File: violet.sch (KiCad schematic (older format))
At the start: 47 parts, among them J1 NEIGHBOR1, J10 Conn_01x08, J2 NEIGHBOR2, J3 NEIGHBOR1, J4 BONUS_ROW, J5 NEIGHBOR2, J6 NEIGHBOR1, J7 BONUS_ROW, J8 BONUS_ROW, J9 NEIGHBOR2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

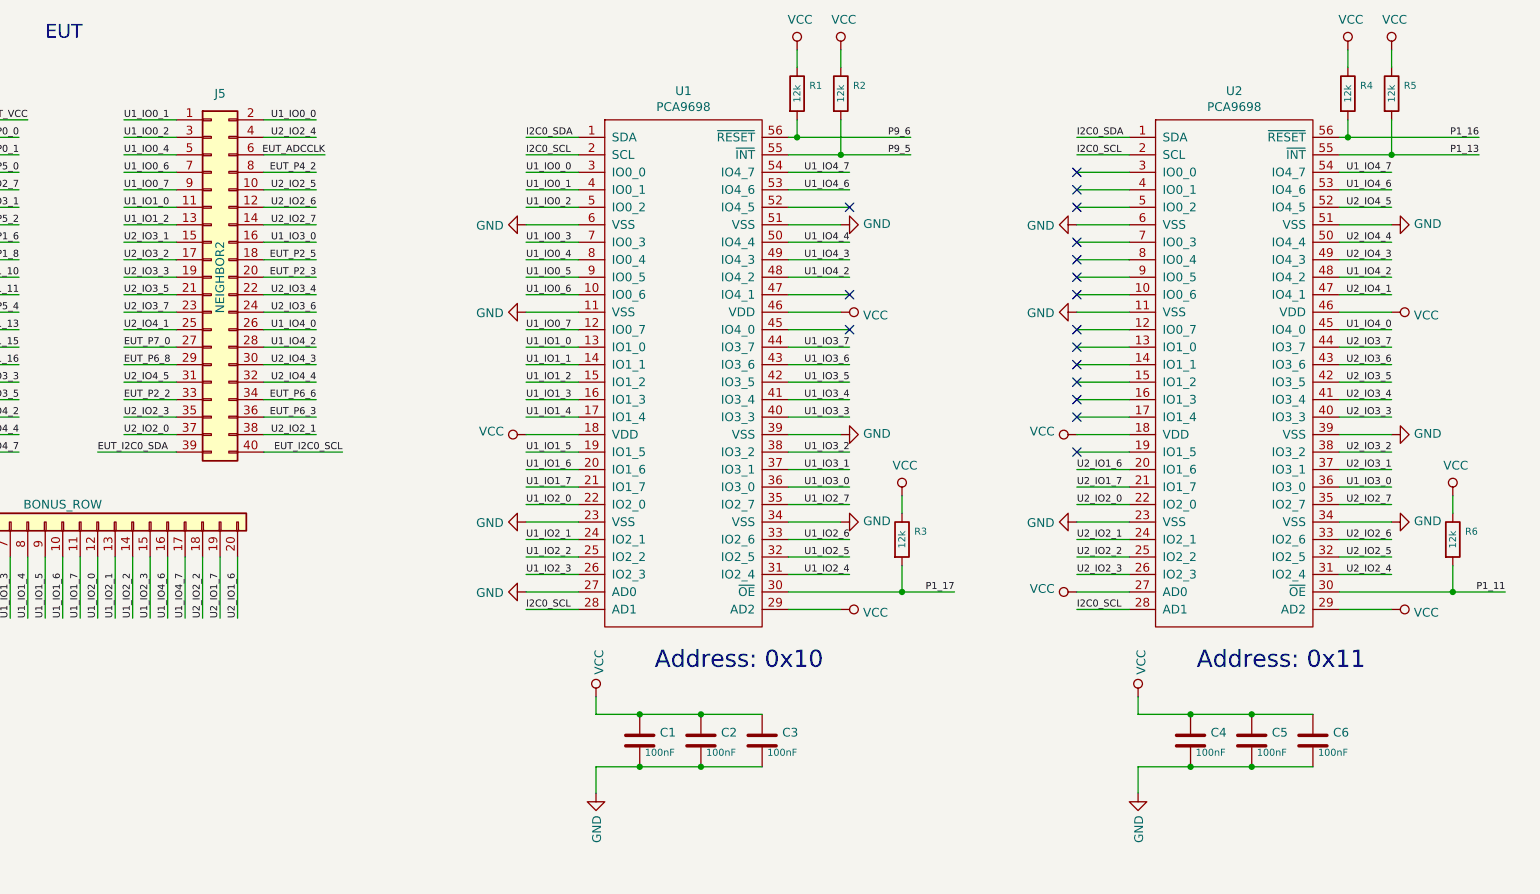
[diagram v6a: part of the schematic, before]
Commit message: Complete routing of PCB; update routing in schematic for ease of routing on PCB
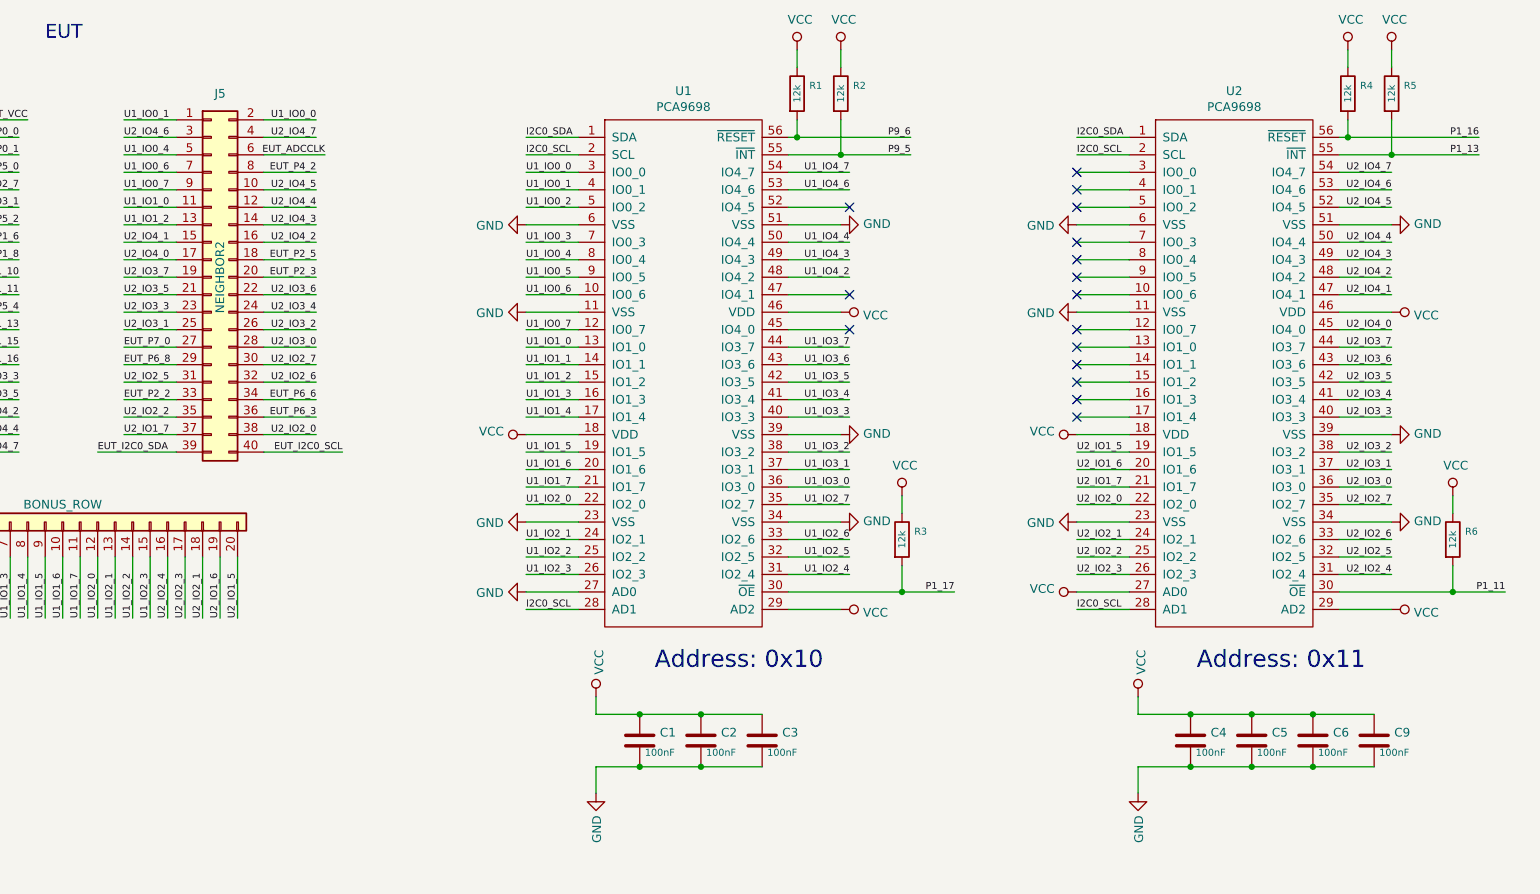
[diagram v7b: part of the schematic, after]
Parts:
- added C9: 100nF, gsg-modules:0603, symbol Device:C
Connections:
- net GND: now also C9.2
- net U1_IO0_2: no longer J5.3 (Pin_3)
- net U1_IO3_0: no longer J5.16 (Pin_16), U2.36 (IO3_0)
- net U1_IO4_2: no longer J5.28 (Pin_28), U2.48 (IO4_2)
- net U1_IO4_6: no longer J4.16 (Pin_16), U2.53 (IO4_6)
- net U1_IO4_7: no longer J4.17 (Pin_17), U2.54 (IO4_7)
- net U2_IO1_6: now also J4.19 (Pin_19); no longer J4.20 (Pin_20)
- net U2_IO1_7: now also J5.37 (Pin_37); no longer J4.19 (Pin_19)
- net U2_IO2_0: now also J5.38 (Pin_38); no longer J5.37 (Pin_37)
- net U2_IO2_1: now also J4.18 (Pin_18); no longer J5.38 (Pin_38)
- net U2_IO2_2: now also J5.35 (Pin_35); no longer J4.18 (Pin_18)
- net U2_IO2_3: now also J4.17 (Pin_17); no longer J5.35 (Pin_35)
- net U2_IO2_4: now also J4.16 (Pin_16); no longer J5.4 (Pin_4)
- net U2_IO2_5: now also J5.31 (Pin_31); no longer J5.10 (Pin_10)
- net U2_IO2_6: now also J5.32 (Pin_32); no longer J5.12 (Pin_12)
- net U2_IO2_7: now also J5.30 (Pin_30); no longer J5.14 (Pin_14)
- net U2_IO3_1: now also J5.25 (Pin_25); no longer J5.15 (Pin_15)
- net U2_IO3_2: now also J5.26 (Pin_26); no longer J5.17 (Pin_17)
- net U2_IO3_3: now also J5.23 (Pin_23); no longer J5.19 (Pin_19)
- net U2_IO3_4: now also J5.24 (Pin_24); no longer J5.22 (Pin_22)
- net U2_IO3_6: now also J5.22 (Pin_22); no longer J5.24 (Pin_24)
- net U2_IO3_7: now also J5.19 (Pin_19); no longer J5.23 (Pin_23)
- net U2_IO4_1: now also J5.15 (Pin_15); no longer J5.25 (Pin_25)
- net U2_IO4_3: now also J5.14 (Pin_14); no longer J5.30 (Pin_30)
- net U2_IO4_4: now also J5.12 (Pin_12); no longer J5.32 (Pin_32)
- net U2_IO4_5: now also J5.10 (Pin_10); no longer J5.31 (Pin_31)
- net VCC: now also C9.1
- net U2_IO1_5: now reaches U2.19 (IO1_5)
- net U2_IO1_5: now also J4.20 (Pin_20)
- net U1_IO4_0 renamed U2_IO4_0
- net U2_IO4_0: now also J5.17 (Pin_17); no longer J5.26 (Pin_26)
- new net U2_IO3_0: J5.28 (Pin_28), U2.36 (IO3_0)
- new net U2_IO4_2: J5.16 (Pin_16), U2.48 (IO4_2)
- new net U2_IO4_6: J5.3 (Pin_3), U2.53 (IO4_6)
- new net U2_IO4_7: J5.4 (Pin_4), U2.54 (IO4_7)
- no-connect marks 170 -> 169
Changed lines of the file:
@@
 Text Label 8750 4050 0    40   ~ 0
 U2_IO2_3
-Text Label 3300 3150 0    40   ~ 0
+Text Label 3650 4300 1    40   ~ 0
 U2_IO2_3
 Text Label 8750 3950 0    40   ~ 0
 U2_IO2_2
-Text Label 3750 4300 1    40   ~ 0
+Text Label 3300 3150 0    40   ~ 0
 U2_IO2_2
 Wire Wire Line
@@
 Text Label 8750 3850 0    40   ~ 0
 U2_IO2_1
-Text Label 4400 3250 2    40   ~ 0
+Text Label 3750 4300 1    40   ~ 0
 U2_IO2_1
 Wire Wire Line
@@
 Wire Wire Line
 	9050 3650 8750 3650
-Text Label 3300 3250 0    40   ~ 0
+Text Label 4400 3250 2    40   ~ 0
 U2_IO2_0
 Wire Wire Line
@@
 Text Label 8750 3550 0    40   ~ 0
 U2_IO1_7
+Text Label 3300 3250 0    40   ~ 0
+U2_IO1_7
 Text Label 3850 4300 1    40   ~ 0
-U2_IO1_7
-Text Label 3950 4300 1    40   ~ 0
 U2_IO1_6
 Wire Wire Line
@@
 Wire Wire Line
 	4100 1550 4400 1550
-Text Label 4400 1950 2    40   ~ 0
+Text Label 4400 2950 2    40   ~ 0
 U2_IO2_6
-Text Label 4400 1550 2    40   ~ 0
+Text Label 3550 4300 1    40   ~ 0
 U2_IO2_4
-Text Label 4400 1850 2    40   ~ 0
+Text Label 3300 2950 0    40   ~ 0
 U2_IO2_5
-Text Label 4400 2050 2    40   ~ 0
+Text Label 4400 2850 2    40   ~ 0
 U2_IO2_7
 Wire Wire Line
@@
 Wire Wire Line
 	3600 1850 3300 1850
-Text Label 3300 2250 0    40   ~ 0
+Text Label 4400 2650 2    40   ~ 0
 U2_IO3_2
-Text Label 3300 2150 0    40   ~ 0
+Text Label 3300 2650 0    40   ~ 0
 U2_IO3_1
-Text Label 3300 2350 0    40   ~ 0
+Text Label 3300 2550 0    40   ~ 0
 U2_IO3_3
 Wire Wire Line
@@
 Wire Wire Line
 	3600 2150 3300 2150
-Text Label 3300 2550 0    40   ~ 0
+Text Label 3300 2350 0    40   ~ 0
 U2_IO3_7
 Wire Wire Line
@@
 Text Label 10550 2950 2    40   ~ 0
 U2_IO3_5
+Text Label 4400 2550 2    40   ~ 0
+U2_IO3_4
 Text Label 4400 2450 2    40   ~ 0
-U2_IO3_4
-Text Label 4400 2550 2    40   ~ 0
 U2_IO3_6
 Wire Wire Line
@@
 Wire Wire Line
 	3300 2350 3600 2350
-Text Label 3300 2650 0    40   ~ 0
+Text Label 3300 2150 0    40   ~ 0
 U2_IO4_1
-Text Label 4400 2850 2    40   ~ 0
+Text Label 4400 2050 2    40   ~ 0
 U2_IO4_3
 Wire Wire Line
@@
 Wire Wire Line
 	3300 2850 3600 2850
-Text Label 4400 2950 2    40   ~ 0
+Text Label 4400 1950 2    40   ~ 0
 U2_IO4_4
-Text Label 3300 2950 0    40   ~ 0
+Text Label 4400 1850 2    40   ~ 0
 U2_IO4_5
 Text Label 10550 2150 2    40   ~ 0
@@
 Wire Wire Line
 	5600 2950 5900 2950
-Text Label 3300 1550 0    40   ~ 0
-U1_IO0_2
+Text Label 8750 3350 0    40   ~ 0
+U2_IO1_5
 Wire Wire Line
 	2700 3150 2400 3150
@@
 U1_IO0_2
 Text Label 10550 3550 2    40   ~ 0
-U1_IO3_0
+U2_IO3_0
+Text Label 4400 2750 2    40   ~ 0
+U2_IO3_0
+Text Label 10550 2650 2    40   ~ 0
+U2_IO4_0
+Text Label 3300 2250 0    40   ~ 0
+U2_IO4_0
+Text Label 10550 2350 2    40   ~ 0
+U2_IO4_2
 Text Label 4400 2150 2    40   ~ 0
-U1_IO3_0
-Text Label 10550 2650 2    40   ~ 0
-U1_IO4_0
-Text Label 4400 2650 2    40   ~ 0
-U1_IO4_0
-Text Label 10550 2350 2    40   ~ 0
-U1_IO4_2
-Text Label 4400 2750 2    40   ~ 0
-U1_IO4_2
+U2_IO4_2
 Text Label 10550 1850 2    40   ~ 0
-U1_IO4_6
-Text Label 3550 4300 1    40   ~ 0
-U1_IO4_6
-Text Label 10550 1750 2    40   ~ 0
-U1_IO4_7
-Text Label 3650 4300 1    40   ~ 0
-U1_IO4_7
-NoConn ~ 8750 3350
+U2_IO4_6
+Text Label 3300 1550 0    40   ~ 0
+U2_IO4_6
+Text Label 4400 1550 2    40   ~ 0
+U2_IO4_7
 NoConn ~ 8750 1750
 NoConn ~ 8750 1850
@@
 Wire Notes Line
 	2050 7500 500  7500
+$Comp
+L Device:C C9
+U 1 1 601130D3
+P 10450 5000
+F 0 "C9" H 10565 5046 50  0000 L CNN
+F 1 "100nF" H 10565 4955 40  0000 C TNN
+F 2 "gsg-modules:0603" H 10488 4850 50  0001 C CNN
+F 3 "~" H 10450 5000 50  0001 C CNN
+F 4 "KEMET" H 10450 5000 50  0001 C CNN "Manufacturer"
+F 5 "C0603C104M4RACTU" H 10450 5000 50  0001 C CNN "Part Number"
+F 6 "CAP CER 0.1UF 16V X7R 0603" H 10450 5000 50  0001 C CNN "Description"
+	1    10450 5000
+	1    0    0    -1
+$EndComp
+Wire Wire Line
+	10100 4850 10450 4850
+Connection ~ 10100 4850
+Wire Wire Line
+	10100 5150 10450 5150
+Connection ~ 10100 5150
+Text Label 10550 1750 2    40   ~ 0
+U2_IO4_7
+Text Label 3950 4300 1    40   ~ 0
+U2_IO1_5
 $EndSCHEMATC
